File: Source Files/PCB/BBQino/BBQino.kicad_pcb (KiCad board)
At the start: 2 copper layers, 68.5 x 53.3 mm, 0 parts

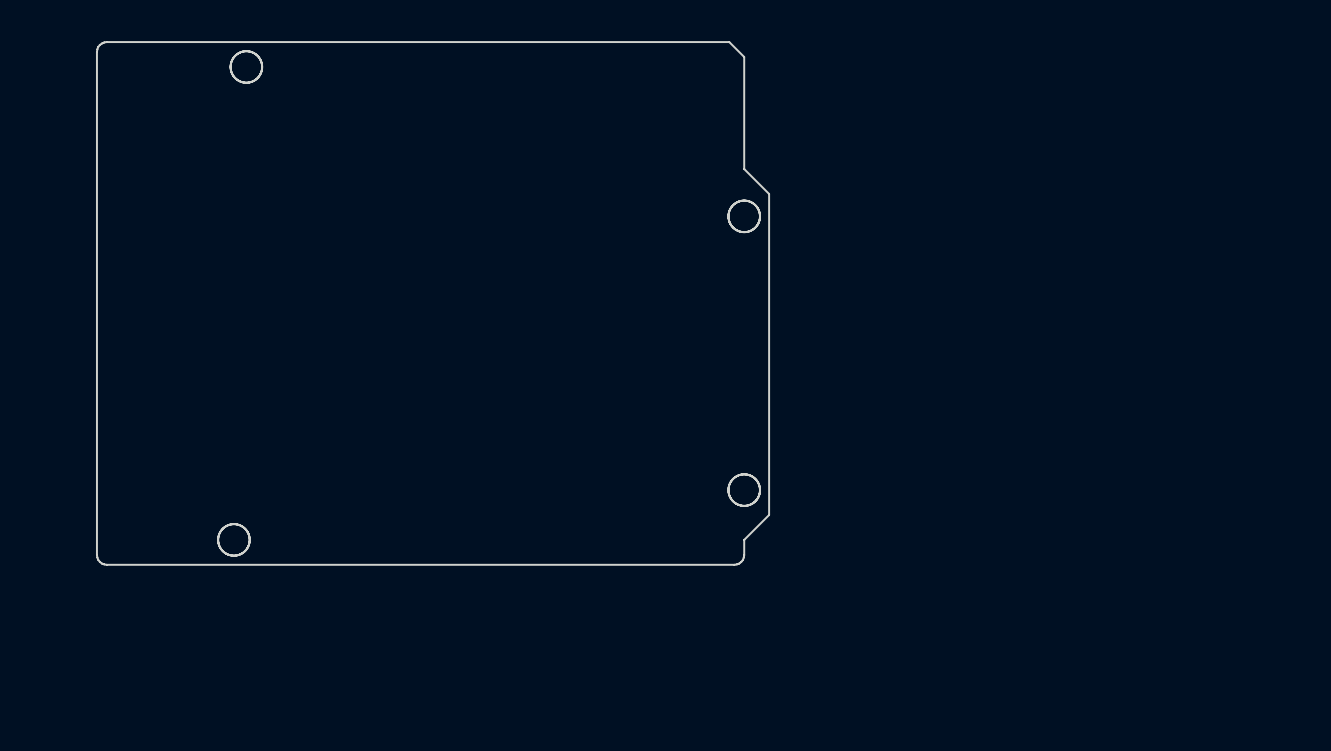
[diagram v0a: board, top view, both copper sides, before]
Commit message: Initial dev on power supplies and arduino configuration. PCB skeleton
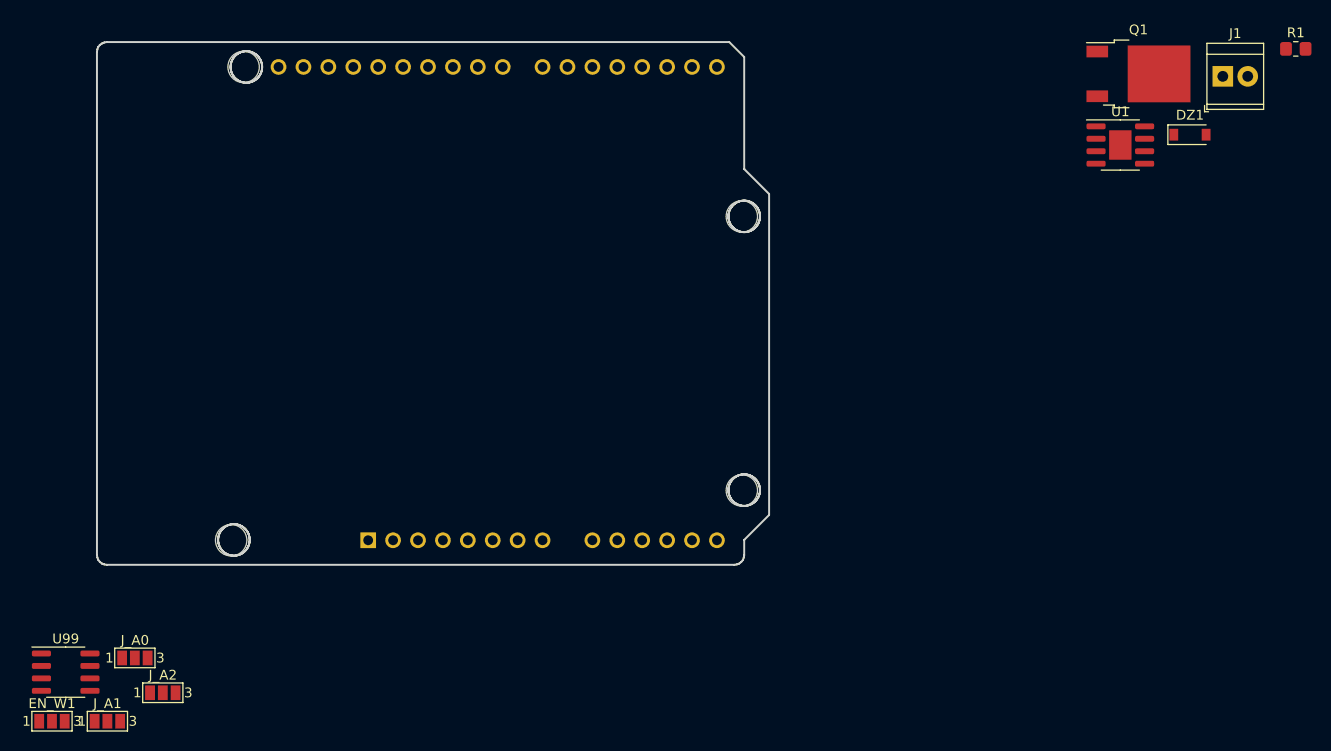
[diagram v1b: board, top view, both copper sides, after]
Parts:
- added A1: Arduino_UNO_R3, BBQino:Arduino_UNO_R3_WithMountingHoles, F.Cu at (78.7, 80.0)
- added DZ1: BZT52C9V1-7-F, Diode_SMD:D_SOD-123, F.Cu at (162.5, 38.7)
- added EN_W1: Jumper_3_Bridged12, Jumper:SolderJumper-3_P1.3mm_Open_Pad1.0x1.5mm_NumberLabels, F.Cu at (46.5, 98.5)
- added J1: VIN < 13V, TerminalBlock_TE-Connectivity:TerminalBlock_TE_282834-2_1x02_P2.54mm_Horizontal, F.Cu at (165.9, 32.7)
- added J_A0: Conn_01x03_Male, Jumper:SolderJumper-3_P1.3mm_Open_Pad1.0x1.5mm_NumberLabels, F.Cu at (55.0, 92.0)
- added J_A1: Conn_01x03_Male, Jumper:SolderJumper-3_P1.3mm_Open_Pad1.0x1.5mm_NumberLabels, F.Cu at (52.1, 98.5)
- added J_A2: Conn_01x03_Male, Jumper:SolderJumper-3_P1.3mm_Open_Pad1.0x1.5mm_NumberLabels, F.Cu at (57.8, 95.6)
- added Q1: IPD068P03L3G, Package_TO_SOT_SMD:TO-252-2, F.Cu at (157.3, 32.5)
- added R1: 600R, Resistor_SMD:R_0805_2012Metric_Pad1.20x1.40mm_HandSolder, F.Cu at (173.3, 29.9)
- added U1: ADP7142ARDZ-5.0, Package_SO:SOIC-8-1EP_3.9x4.9mm_P1.27mm_EP2.29x3mm, F.Cu at (155.4, 39.7)
- added U99: 24LC512, Package_SO:SOIC-8_3.9x4.9mm_P1.27mm, F.Cu at (47.9, 93.5)

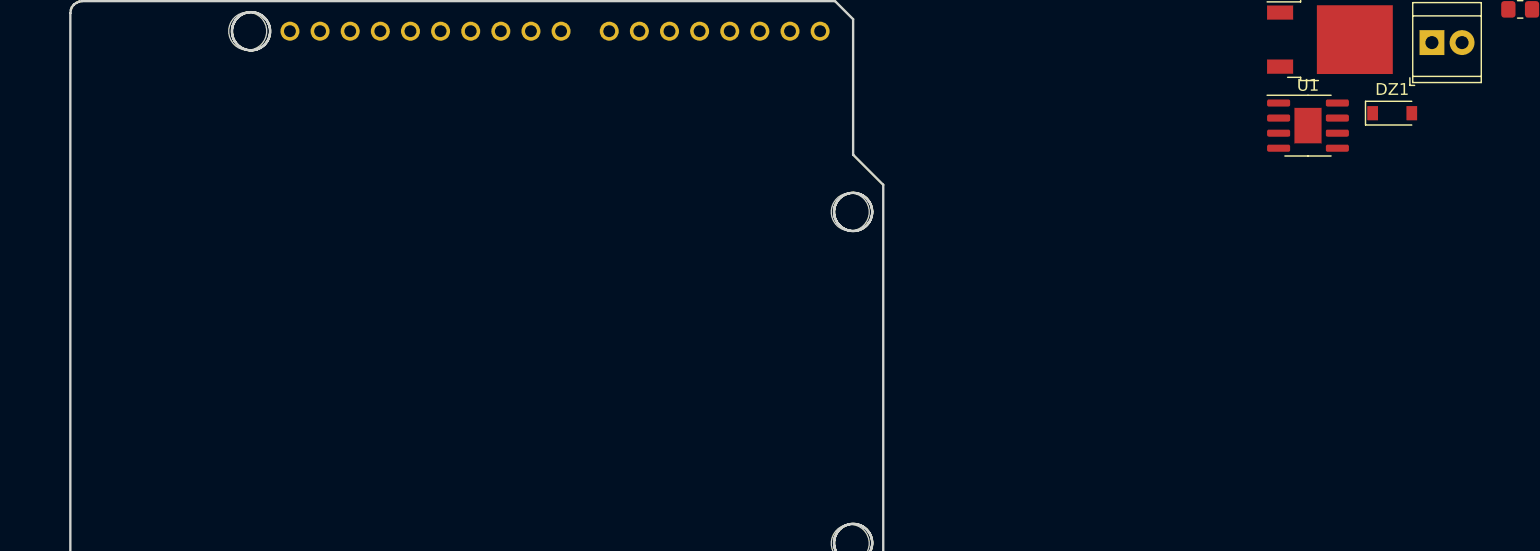
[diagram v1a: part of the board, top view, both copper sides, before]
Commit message: 230V section first Draft. Added external module on top of the shield for the 230V section
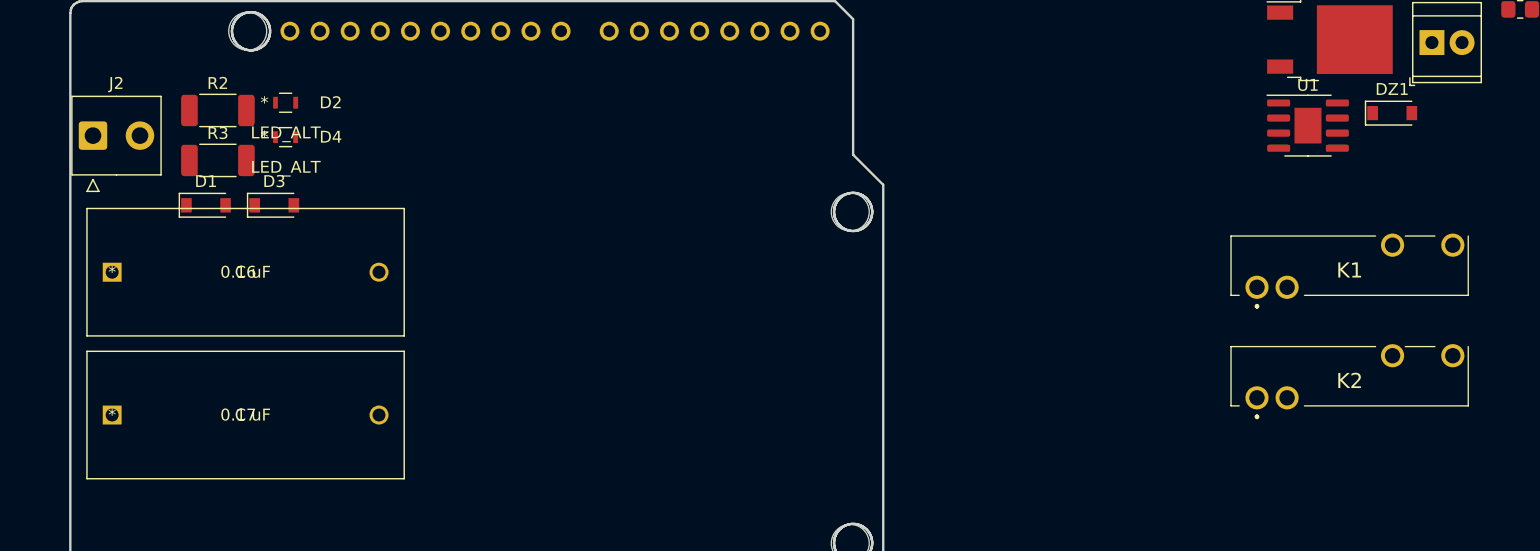
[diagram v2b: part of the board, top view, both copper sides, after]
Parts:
- added C6: 0.1 uF, BBQino:ECWFE2J105K, F.Cu at (54.6, 52.1)
- added C7: 0.1 uF, BBQino:ECWFE2J105K, F.Cu at (54.6, 64.1)
- added D1: 1N4148W-HF, Diode_SMD:D_SOD-123, F.Cu at (62.5, 46.4)
- added D2: LED_ALT, BBQino:150080BS75000, F.Cu at (69.2, 37.8)
- added D3: 1N4148W-HF, Diode_SMD:D_SOD-123, F.Cu at (68.3, 46.4)
- added D4: LED_ALT, BBQino:150080BS75000, F.Cu at (69.2, 40.7)
- added J2: 230V input, Connector_TE-Connectivity:TE_826576-2_1x02_P3.96mm_Vertical, F.Cu at (53.0, 40.6)
- added K1: FTR-MYAA005D, BBQino:FTRMYAA005D, F.Cu at (151.1, 53.3)
- added K2: FTR-MYAA005D, BBQino:FTRMYAA005D, F.Cu at (151.1, 62.7)
- added R2: 22k, Resistor_SMD:R_2010_5025Metric_Pad1.40x2.65mm_HandSolder, F.Cu at (63.5, 38.4)
- added R3: 22k, Resistor_SMD:R_2010_5025Metric_Pad1.40x2.65mm_HandSolder, F.Cu at (63.5, 42.6)
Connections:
- A1 pad 29: Net-(A1-Pad29) -> GNDD
- A1 pad 6: Net-(A1-Pad6) -> GNDD
- A1 pad 7: Net-(A1-Pad7) -> GNDD

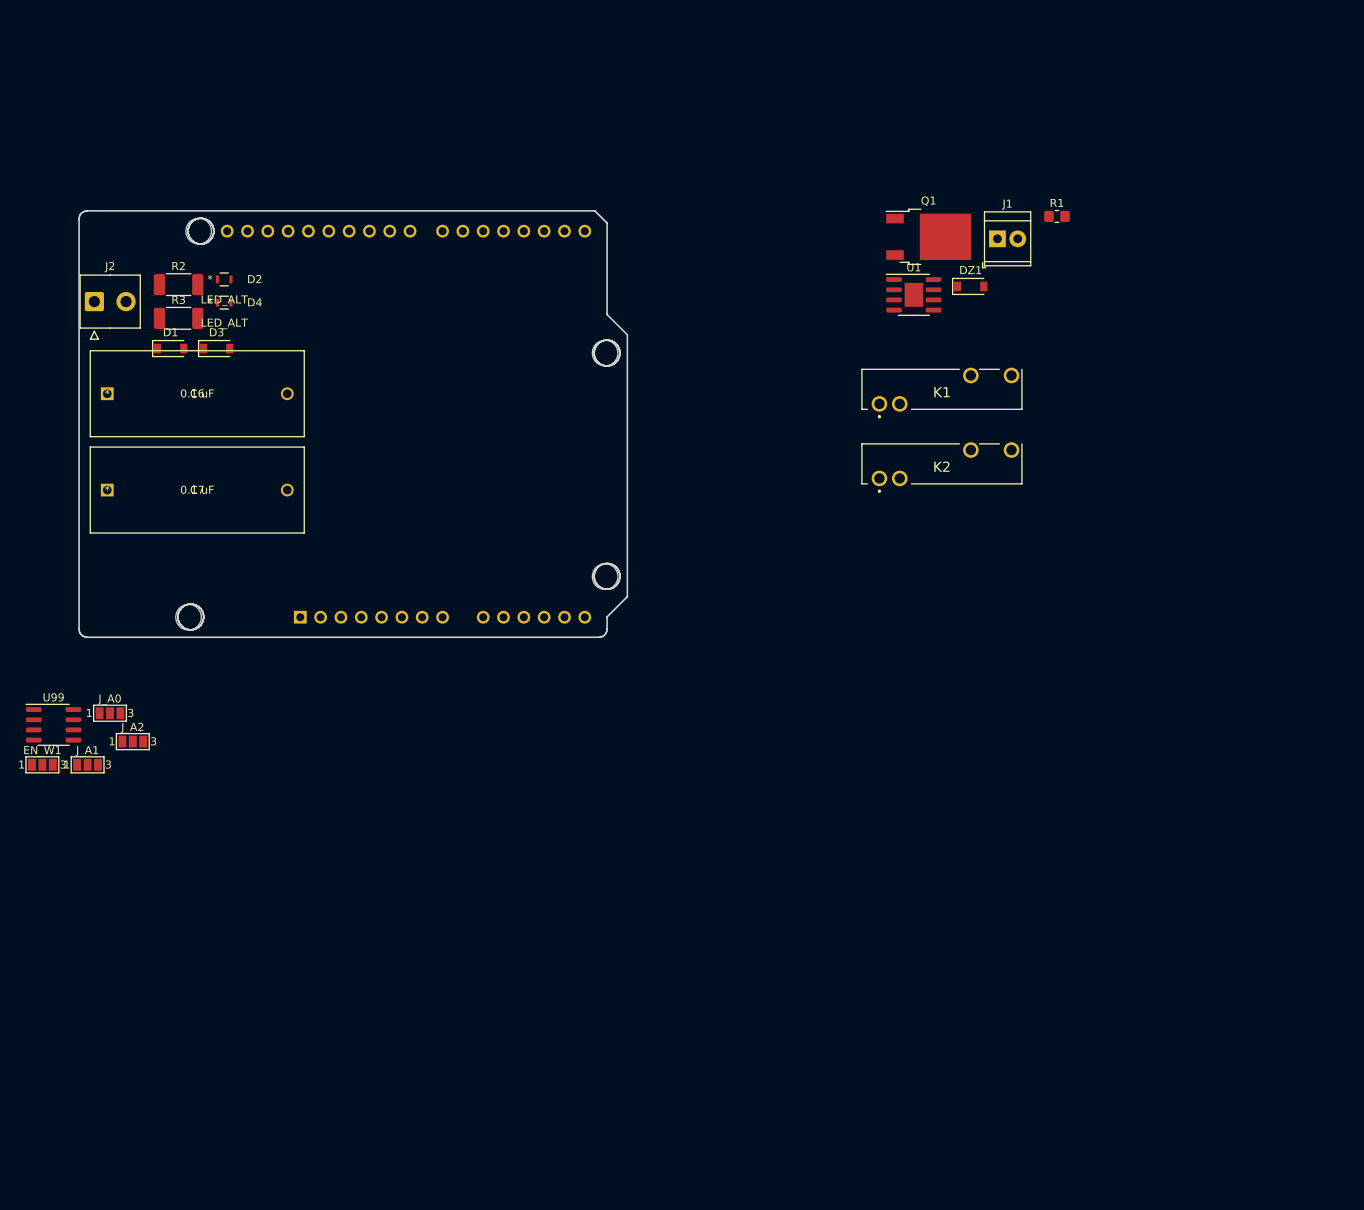
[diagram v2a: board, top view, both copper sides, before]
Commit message: Updated PCB external module
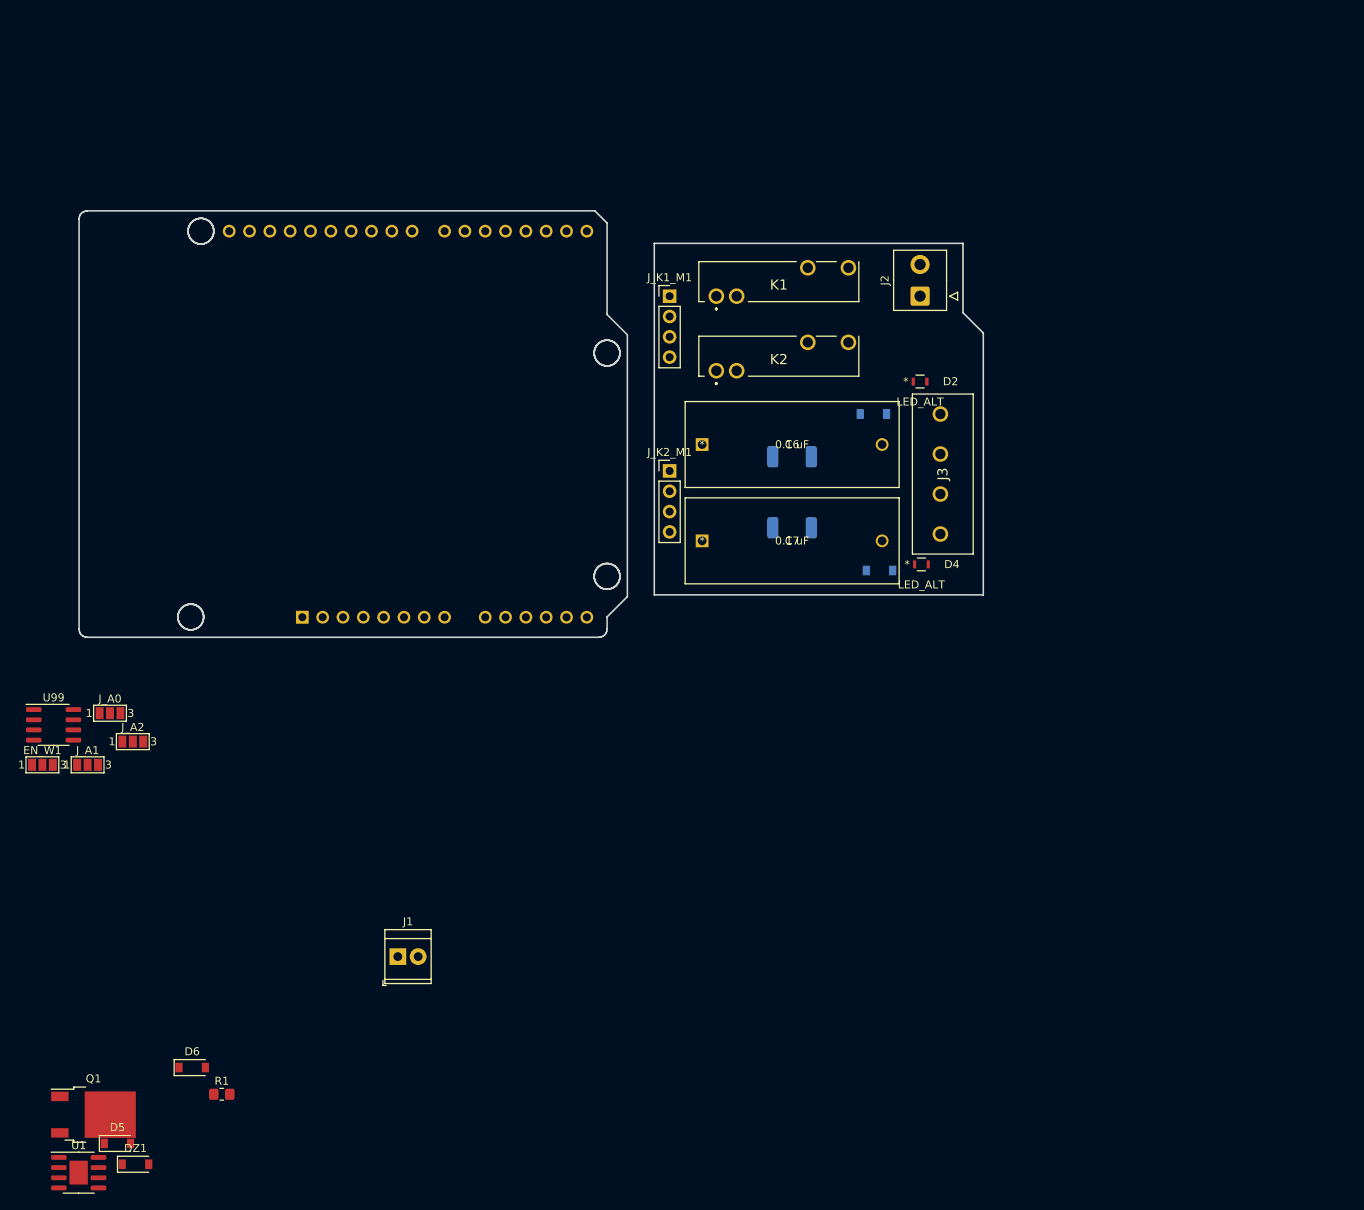
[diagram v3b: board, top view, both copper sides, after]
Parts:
- added D5: 1N4148W-HF, Diode_SMD:D_SOD-123, F.Cu at (55.9, 145.8)
- added D6: 1N4148W-HF, Diode_SMD:D_SOD-123, F.Cu at (65.2, 136.3)
- added J3: 230V out, BBQino:TB00250004BE, F.Cu at (158.8, 54.6)
- added J_K1_M1: Conn_01x04_Female, Connector_PinHeader_2.54mm:PinHeader_1x04_P2.54mm_Vertical, F.Cu at (124.9, 39.9)
- added J_K2_M1: Conn_01x04_Female, Connector_PinHeader_2.54mm:PinHeader_1x04_P2.54mm_Vertical, F.Cu at (124.9, 61.7)
- A1: footprint BBQino:Arduino_UNO_R3_WithMountingHoles -> Module:Arduino_UNO_R3_WithMountingHoles; moved to B.Cu
- D1, D3, R2, R3: moved to B.Cu
- moved DZ1 151.5 mm to (58.1, 148.4)
- moved R1 151.5 mm to (68.9, 139.6)
- moved Q1 151.5 mm to (52.9, 142.2)
- moved U1 151.5 mm to (51.0, 149.4)
- moved J1 116.9 mm to (90.9, 122.4)
- moved J2 103.2 mm to (156.2, 39.9), turned to 90 degrees
- moved D4 93.1 mm to (156.4, 73.4)
- moved D1 88.2 mm to (150.4, 54.6)
- moved D2 87.9 mm to (156.2, 50.5)
- moved D3 87.4 mm to (151.1, 74.2)
- moved R3 81.0 mm to (140.2, 68.8)
- moved R2 79.6 mm to (140.2, 59.9)
- moved C6 74.6 mm to (129.0, 58.4)
- moved C7 74.6 mm to (129.0, 70.5)
- moved K1 24.4 mm to (130.7, 39.9)
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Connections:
- K1 pad 3: Net-(K1-Pad3) -> 230V_L
- K1 pad 4: Net-(K1-Pad4) -> 230V_OUT_1
- K2 pad 3: Net-(K2-Pad3) -> 230V_L
- K2 pad 4: Net-(K2-Pad4) -> 230V_OUT_2
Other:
- board size 68.5 x 53.3 mm -> 113 x 53.3 mm
